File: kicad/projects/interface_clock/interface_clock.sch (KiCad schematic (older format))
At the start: 41 parts, among them J1 Control_signal_backplane, J2 Aux_connection, J3 Bus_connection, J4 MAR_content_in, J5 Conn_02x18_Odd_Even, J6 Conn_01x05_Female, U1 74HC109, U10 74HC245, U11 74HC245, U2 74HC04, U3 74HC00, U4 74HC126, U5 74HC27, U6 74HC00, U7 74HC245, U8 74HC245, U9 74HC109

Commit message: Bits and pieces in CPU interface and clock board.
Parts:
- removed J5: Conn_02x18_Odd_Even, Connector_PinSocket_2.54mm:PinSocket_2x18_P2.54mm_Vertical, symbol Connector_Generic:Conn_02x18_Odd_Even
- added J5: EXT_BUS, Connector_PinSocket_2.54mm:PinSocket_1x16_P2.54mm_Vertical, symbol Connector:Conn_01x16_Female
- added J7: CLOCK_RWMEM_OUT, Connector_PinSocket_2.54mm:PinSocket_1x04_P2.54mm_Vertical, symbol Connector:Conn_01x04_Female
- added J8: EXT_ADDR, Connector_PinSocket_2.54mm:PinSocket_1x16_P2.54mm_Vertical, symbol Connector:Conn_01x16_Female
- J6: value Conn_01x05_Female -> CONTROL_INPUTS
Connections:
- net labels added: DATA_CLK_OUT, ENABLE_CLK_OUTPUT, EXT_CLK_IN
- net labels removed: DATA_CLOCK_OUT, ENABLE_CLOCK_OUTPUT, EXT_CLOCK_IN
- wire segments 226 -> 237
- no-connect marks 6 -> 35
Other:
- moved on the sheet: J3, J4

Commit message: PCB work for interface.
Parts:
- removed C11: 0.1uF, Capacitor_THT:C_Disc_D4.7mm_W2.5mm_P5.00mm, symbol Device:C
- removed R1, R2, R3, R4: 10K, Resistor_THT:R_Axial_DIN0207_L6.3mm_D2.5mm_P10.16mm_Horizontal, symbol Device:R_US
- removed U1, U9: 74HC109, Package_DIP:DIP-16_W7.62mm, symbol sixteen-bit-computer:74HC109
- removed U3, U6: 74HC00, Package_DIP:DIP-14_W7.62mm, symbol 74xx:74HC00
- removed U4: 74HC126, Package_DIP:DIP-14_W7.62mm, symbol sixteen-bit-computer:74HC126
- removed U5: 74HC27, Package_DIP:DIP-14_W7.62mm, symbol sixteen-bit-computer:74HC27
- added U1, U5: 74HC02, Package_DIP:DIP-14_W7.62mm, symbol 74xx:74HC02
- added U10: 74HC157, Package_DIP:DIP-16_W7.62mm, symbol sixteen-bit-computer:74HC157
- added U3, U4: 74HC08, Package_DIP:DIP-14_W7.62mm, symbol sixteen-bit-computer:74HC08
- added X1: CXO_DIP8, Oscillator:Oscillator_DIP-8, symbol Oscillator:CXO_DIP8
- renumbered U7 to U6, U8 to U7, U10 to U8, U11 to U9
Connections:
- net labels added: CHOSEN_CLOCK, CLOCK_SEL, CRYSTAL, ENABLE_ADDRESS_BUS_OUTPUT, ENABLE_DATA_BUS_OUTPUT, R_FM_MEM_SAFE, W_TO_MEM_SAFE, ~ENABLE_ADDRESS_BUS_OUTPUT
- net labels removed: CTL_CLK_OUT, DATA_CLK_OUT, ENABLE_BUS_OUTPUT, ENABLE_CLK_OUTPUT, ENABLE_RW_MEM_OUTPUT, R_FM_MEM_OUT, W_TO_MEM_OUT, ~CLK_ENABLE, ~DATA_BUS_OE, ~ENABLE_BUS_OUTPUT, ~RESET, ~R_FM_MEM
- wire segments 237 -> 167
- no-connect marks 35 -> 33
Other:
- note removed: "OR GATE"
- moved on the sheet: C10, C12, C13, C14, C4, C5, C6, C7, C8, C9, J1, J2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

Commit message: Add LED outputs to interface/clock.
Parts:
- added C11, C15, C16: 0.1uF, Capacitor_THT:C_Disc_D4.7mm_W2.5mm_P5.00mm, symbol Device:C
- added D1, D2, D3, D4, D5, D6: LED, sixteen-bit-computer:LED_D5.0mm_Horizontal_O3.81mm_Z3.0mm, symbol Device:LED
- added J9: Conn_01x03_Male, Connector_PinHeader_2.54mm:PinHeader_1x03_P2.54mm_Horizontal, symbol Connector:Conn_01x03_Male
- added R1, R18: 10K, Resistor_THT:R_Axial_DIN0207_L6.3mm_D2.5mm_P10.16mm_Horizontal, symbol Device:R_US
- added R10, R11, R12, R13, R14, R15, R16, R17, R2, R3, R4, R5, R6, R7, R8, R9: R_US, Resistor_THT:R_Axial_DIN0207_L6.3mm_D2.5mm_P10.16mm_Horizontal, symbol Device:R_US
- added U11: 74HC14, Package_DIP:DIP-14_W7.62mm, symbol 74xx:74HC14
- added U12: 74HC245, Package_DIP:DIP-20_W7.62mm, symbol sixteen-bit-computer:74HC245
- J6: footprint Connector_PinSocket_2.54mm:PinSocket_1x05_P2.54mm_Horizontal -> Connector_PinSocket_2.54mm:PinSocket_1x06_P2.54mm_Horizontal; symbol Connector:Conn_01x05_Female -> Connector:Conn_01x06_Female
- J7: footprint Connector_PinSocket_2.54mm:PinSocket_1x04_P2.54mm_Vertical -> Connector_PinSocket_2.54mm:PinSocket_1x04_P2.54mm_Horizontal
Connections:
- net labels added: EXT_RESET, LED_CONTROL
- wire segments 167 -> 249
- no-connect marks 33 -> 36
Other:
- note added: "Reset on powerup"
- note added: "Safety net for preventing simultaneous read and write to mem"
- moved on the sheet: C10, C12, C13, C14, J2, J7, RN5, RN6, U10, U1C, U1D, U3A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

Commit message: Most of interface positioning complete.
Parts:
- removed R10, R11: R_US, Resistor_THT:R_Axial_DIN0207_L6.3mm_D2.5mm_P10.16mm_Horizontal, symbol Device:R_US
- added C17: 0.1uF, Capacitor_THT:C_Disc_D4.7mm_W2.5mm_P5.00mm, symbol Device:C
- added D7, D8: LED, sixteen-bit-computer:LED_D5.0mm_Horizontal_O3.81mm_Z3.0mm, symbol Device:LED
- added J10: Conn_01x02_Female, Connector_PinSocket_2.54mm:PinSocket_1x02_P2.54mm_Horizontal, symbol Connector:Conn_01x02_Female
- added U13: 74HC126, Package_DIP:DIP-14_W7.62mm, symbol sixteen-bit-computer:74HC126
- R1: value 10K -> R_US
- renumbered R2 to R10, R3 to R11, R4 to R12, R5 to R13, R6 to R14, R7 to R15, R12 to R2, R13 to R3, R14 to R4, R15 to R5, R16 to R6, R17 to R7
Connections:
- net CTL_CLK: now also U13.6; no longer U2.4
- net DATA_CLK: now also U13.3; no longer U2.3, U3.11
- net ENABLE_ADDRESS_BUS_OUTPUT: now also U12.9 (A8); no longer U12.7 (A6)
- net ENABLE_DATA_BUS_OUTPUT: now also U12.8 (A7); no longer U12.6 (A5)
- net GND: now also R1.1, R2.2, R3.2, R4.2, R5.2, R6.2, R7.2, R8.2, C17.2, J10.2 (Pin_2), U13.10, U13.12, U13.13, U13.7 (GND), U13.9; no longer R8.1, R9.1
- net VCC: now also R9.1, C17.1, J10.1 (Pin_1), U13.1, U13.14 (VCC), U13.4; no longer R1.1
- net at C15.1, U11.1: now also R9.2; no longer R1.2
- net at U12.11 (B8): now also D8.2 (A)
- net at U12.12 (B7): now also D7.2 (A)
- net at D1.1 (K): now also R1.2; no longer R2.1
- net at D2.1 (K): now also R2.1; no longer R3.1
- net at D3.1 (K): now also R3.1; no longer R4.1
- net at D4.1 (K): now also R4.1; no longer R5.1
- net at D5.1 (K): now also R5.1; no longer R6.1
- net at D6.1 (K): now also R6.1; no longer R7.1
- new net: D7.1 (K), R7.1
- new net: D8.1 (K), R8.1
- new net UNBUF_CTL_CLK: U12.6 (A5), U13.5, U2.4
- new net UNBUF_DATA_CLK: U12.7 (A6), U13.2, U2.3, U3.11
- no-connect marks 36 -> 38
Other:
- moved on the sheet: C1, C11, C2, C3, C4, C5, R1, R2, R3, R4, R5, R6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

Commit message: Interface clock ready for tech checks.
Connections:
- net EXT_RESET: no longer U12.2 (A1)
- net RESET: now also U12.2 (A1)
- net ADDR_BUS_OE: now reaches D8.2 (A), U12.11 (B8)
- net DATA_BUS_OE_LED: now reaches D7.2 (A), U12.12 (B7)
- net DATA_CLK_LED: now reaches D6.2 (A), U12.13 (B6)
- net CTL_CLK_LED: now reaches D5.2 (A), U12.14 (B5)
- net CLK_ENABLE_LED: now reaches D4.2 (A), U12.15 (B4)
- net CLOCK_SEL_LED: now reaches D3.2 (A), U12.16 (B3)
- net CLK_IN_LED: now reaches D2.2 (A), U12.17 (B2)
- net RESET_LED: now reaches D1.2 (A), U12.18 (B1)
- net ENABLE_ADDRESS_BUS_OUTPUT renamed ADDRESS_BUS_OUTPUT_ENABLE
- net ENABLE_DATA_BUS_OUTPUT renamed DATA_BUS_OUTPUT_ENABLE
- net ~ENABLE_ADDRESS_BUS_OUTPUT renamed ~ADDRESS_BUS_OUTPUT_ENABLE
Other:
- moved on the sheet: D1, D2, D3, D4, D5, D6, D7, D8, R1, R2, R3, R4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

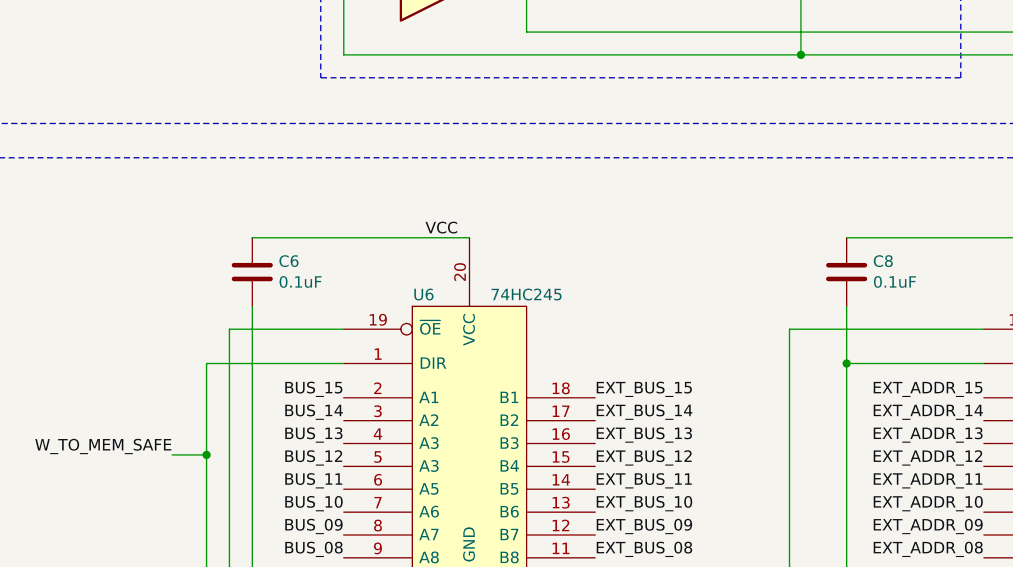
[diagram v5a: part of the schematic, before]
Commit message: Add bus out pullup resistors to interface.
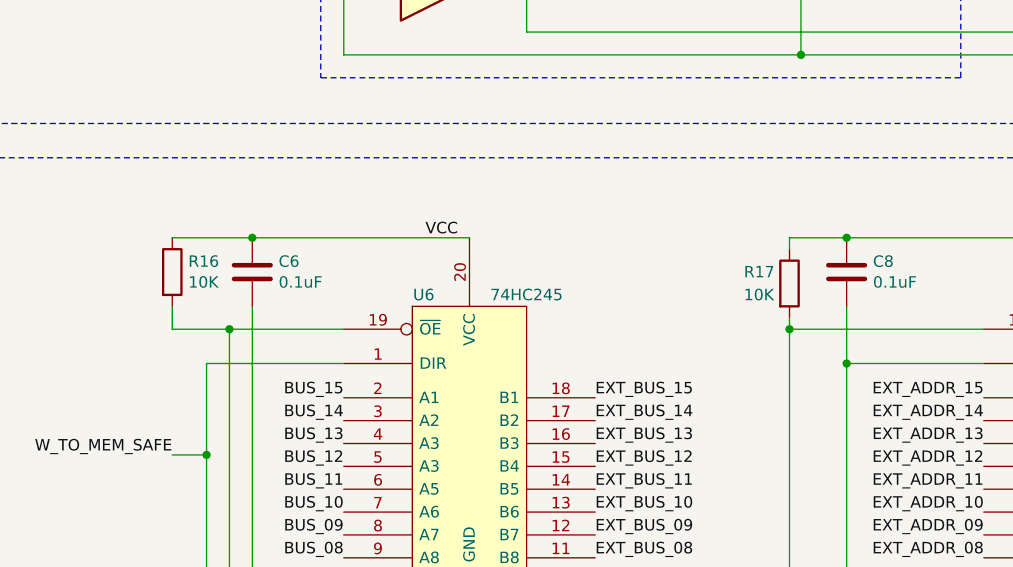
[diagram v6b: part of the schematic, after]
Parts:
- added R16, R17: 10K, Resistor_THT:R_Axial_DIN0207_L6.3mm_D2.5mm_P10.16mm_Horizontal, symbol Device:R
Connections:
- net VCC: now also R16.1, R17.1
- net ~ADDRESS_BUS_OUTPUT_ENABLE: now also R17.2
- net at U5.1, U6.19 (~OE), U7.19 (~OE): now also R16.2
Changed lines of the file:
@@
 Wire Wire Line
 	15000 8750 15450 8750
+$Comp
+L Device:R R16
+U 1 1 63709FE1
+P 3000 3600
+F 0 "R16" H 3070 3646 50  0000 L CNN
+F 1 "10K" H 3070 3555 50  0000 L CNN
+F 2 "Resistor_THT:R_Axial_DIN0207_L6.3mm_D2.5mm_P10.16mm_Horizontal" V 2930 3600 50  0001 C CNN
+F 3 "~" H 3000 3600 50  0001 C CNN
+	1    3000 3600
+	1    0    0    -1
+$EndComp
+$Comp
+L Device:R R17
+U 1 1 6370AB2E
+P 5700 3650
+F 0 "R17" H 5500 3700 50  0000 L CNN
+F 1 "10K" H 5500 3600 50  0000 L CNN
+F 2 "Resistor_THT:R_Axial_DIN0207_L6.3mm_D2.5mm_P10.16mm_Horizontal" V 5630 3650 50  0001 C CNN
+F 3 "~" H 5700 3650 50  0001 C CNN
+	1    5700 3650
+	1    0    0    -1
+$EndComp
+Connection ~ 5700 3850
+Wire Wire Line
+	5700 3450 5950 3450
+Connection ~ 5950 3450
+Wire Wire Line
+	5700 3850 5700 3800
+Wire Wire Line
+	5700 3450 5700 3500
+Wire Wire Line
+	3250 3850 3000 3850
+Wire Wire Line
+	3000 3850 3000 3750
+Connection ~ 3250 3850
+Wire Wire Line
+	3000 3450 3350 3450
+Connection ~ 3350 3450
 $EndSCHEMATC

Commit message: Add HC109 chip. Add simpler clock and reset delay to interface. Need to lay out on PCB.
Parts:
- added C18: 0.1uF, Capacitor_THT:C_Disc_D4.7mm_W2.5mm_P5.00mm, symbol Device:C
- added C19: C, Capacitor_THT:C_Disc_D4.7mm_W2.5mm_P5.00mm, symbol Device:C
- added R19: R_US, Resistor_THT:R_Axial_DIN0207_L6.3mm_D2.5mm_P10.16mm_Horizontal, symbol Device:R_US
- added U14: 74HC109, Package_DIP:DIP-16_W7.62mm, symbol sixteen-bit-computer:74HC109
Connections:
- net CHOSEN_CLOCK: no longer U3.13
- net CLK_ENABLE: now also U3.5; no longer U4.2
- net GND: now also U2.5, U3.12, U3.13, U4.1, U4.2, C18.2, C19.2, U14.12 (C), U14.13 (~K), U14.14 (J), U14.3 (~K), U14.8 (GND); no longer U11.5, U11.9
- net HALT: now also U1.6; no longer U2.1
- net RESET: now also U2.3, U3.8; no longer U11.4, U2.5
- net SCE_OUT: now also U14.4 (C); no longer U1.9
- net UNBUF_CTL_CLK: now also U14.7 (~Q); no longer U2.4
- net UNBUF_DATA_CLK: now also U14.6 (Q); no longer U2.3, U3.11
- net VCC: now also C18.1, U14.11 (~PRE), U14.15 (~CLR), U14.16 (VCC), U14.2 (J), U14.5 (~PRE)
- net CLK_EN_FROM_RESET: now reaches U2.2
- net CLK_EN_FROM_RESET: now also U1.5; no longer U4.1
- net at U2.6: no longer U3.5
- net at U1.2, U2.10: no longer U3.9
- net at U1.12, U2.12: no longer U3.10
- net at U1.10: now also U2.1; no longer U1.6
- net at U3.4: now also U1.4; no longer U4.3
- net at U11.6: now also U1.8, U3.9
- net at U11.8: now also U11.5
- new net: U14.1 (~CLR), U2.4
- new net: C19.1, R19.2, U11.9
- new net RESET_PWRUP: R19.1, U1.9, U11.4, U3.10
- no-connect marks 38 -> 42
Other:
- note added: "Reset signal disabling clock"
- moved on the sheet: C12, C13, C14, C16, D1, D2, D3, D4, D5, D6, D7, D8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

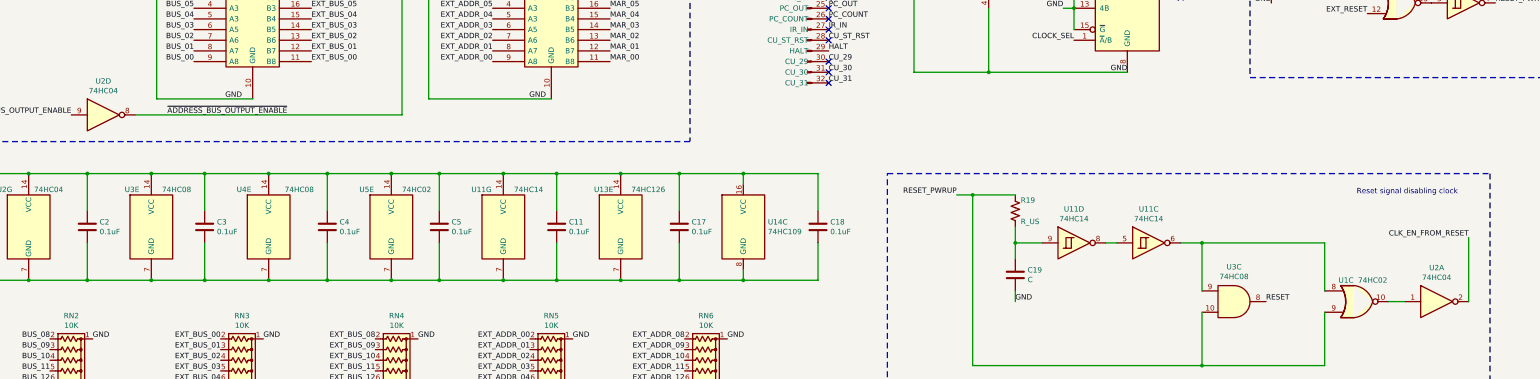
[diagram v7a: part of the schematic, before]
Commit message: Finish wiring on interface.
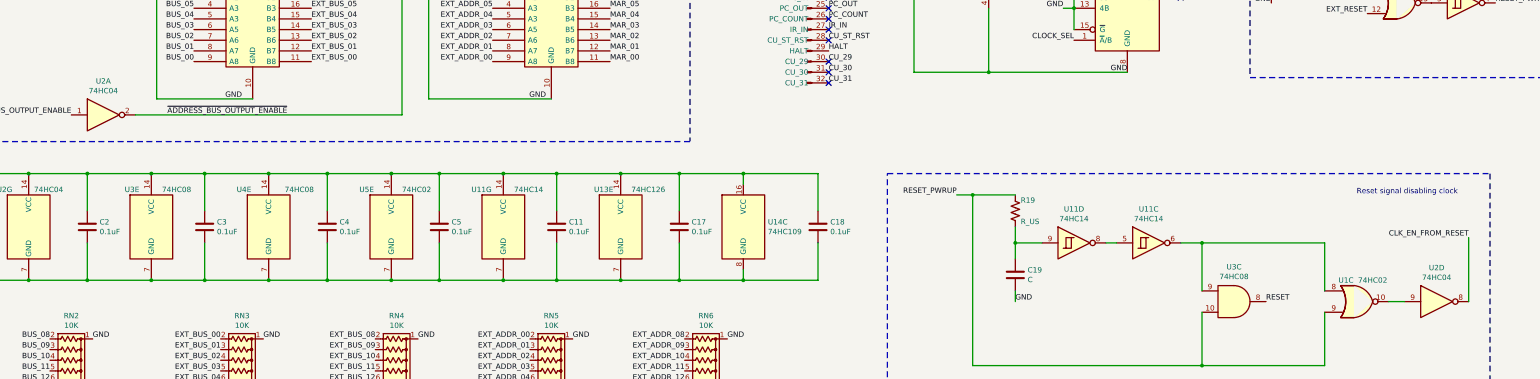
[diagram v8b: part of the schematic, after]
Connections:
- net ADDRESS_BUS_OUTPUT_ENABLE: now also U2.1; no longer U2.9
- net CLK_EN_FROM_RESET: now also U2.8; no longer U2.2
- net ~ADDRESS_BUS_OUTPUT_ENABLE: now also U2.2; no longer U2.8
- net at U1.10: now also U2.9; no longer U2.1
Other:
- moved on the sheet: U2A, U2D
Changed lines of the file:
@@
 L 74xx:74HC04 U2
 U 1 1 5FDA77B5
-P 15400 9050
-F 0 "U2" H 15400 9367 50  0000 C CNN
-F 1 "74HC04" H 15400 9276 50  0000 C CNN
-F 2 "Package_DIP:DIP-14_W7.62mm" H 15400 9050 50  0001 C CNN
-F 3 "https://assets.nexperia.com/documents/data-sheet/74HC_HCT04.pdf" H 15400 9050 50  0001 C CNN
-	1    15400 9050
+P 2900 7300
+F 0 "U2" H 2900 7617 50  0000 C CNN
+F 1 "74HC04" H 2900 7526 50  0000 C CNN
+F 2 "Package_DIP:DIP-14_W7.62mm" H 2900 7300 50  0001 C CNN
+F 3 "https://assets.nexperia.com/documents/data-sheet/74HC_HCT04.pdf" H 2900 7300 50  0001 C CNN
+	1    2900 7300
 	1    0    0    -1
 $EndComp
@@
 L 74xx:74HC04 U2
 U 4 1 5FDABC36
-P 2900 7300
-F 0 "U2" H 2900 7617 50  0000 C CNN
-F 1 "74HC04" H 2900 7526 50  0000 C CNN
-F 2 "Package_DIP:DIP-14_W7.62mm" H 2900 7300 50  0001 C CNN
-F 3 "https://assets.nexperia.com/documents/data-sheet/74HC_HCT04.pdf" H 2900 7300 50  0001 C CNN
-	4    2900 7300
+P 15400 9050
+F 0 "U2" H 15400 9367 50  0000 C CNN
+F 1 "74HC04" H 15400 9276 50  0000 C CNN
+F 2 "Package_DIP:DIP-14_W7.62mm" H 15400 9050 50  0001 C CNN
+F 3 "https://assets.nexperia.com/documents/data-sheet/74HC_HCT04.pdf" H 15400 9050 50  0001 C CNN
+	4    15400 9050
 	1    0    0    -1
 $EndComp
